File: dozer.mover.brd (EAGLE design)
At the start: 84.8 x 55.9 mm, 12 parts, among them IC1 PIC18F4550_40, U1 L298, U2 L298

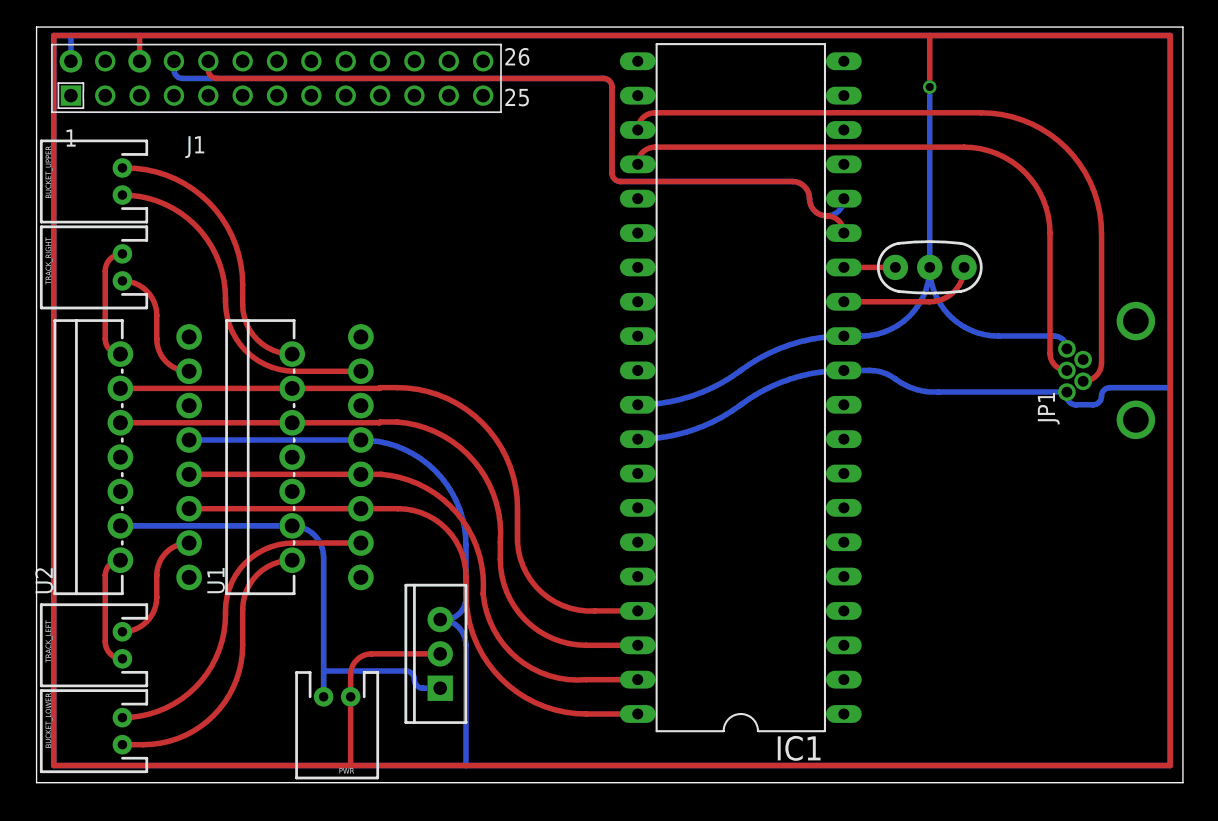
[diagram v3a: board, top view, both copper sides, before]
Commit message: Migrate motor controls further down interface B, frees up GPIO to use for ICSP without having to add loads of resistors. Also added reset circuit required to make PIC run, but not actually a reset switch.
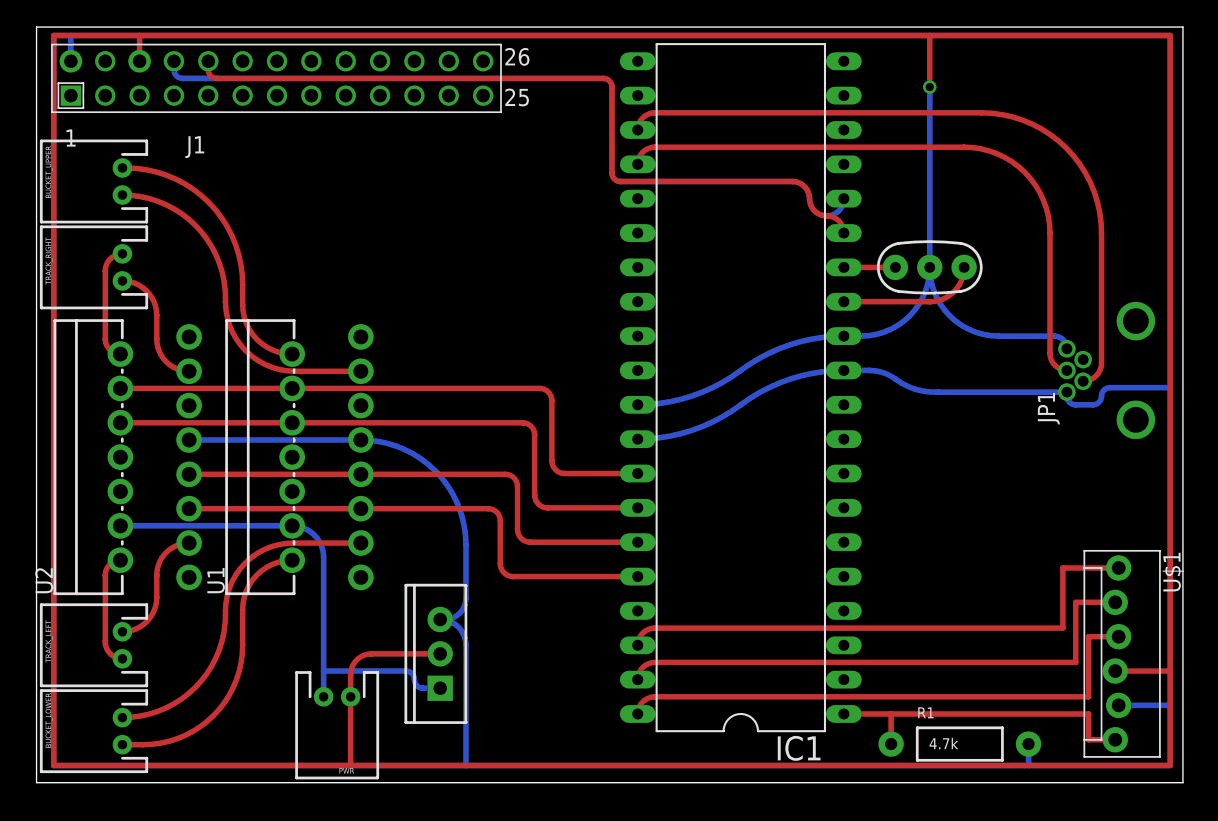
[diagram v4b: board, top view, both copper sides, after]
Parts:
- added R1: 4.7k, SparkFun-Resistors:AXIAL-0.4
- added U$1: PIC-ICSPPOLAR_LOCK, SparkFun-Connectors:MOLEX-1X6_LOCK
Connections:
- removed net N$10: IC1.33
- removed net N$7: IC1.36
- removed net N$8: IC1.35
- removed net N$9: IC1.34
- new net CSSPP: IC1.37
- new net PGC: IC1.39, U$1.2
- new net PGD: IC1.40, U$1.3
- new net PGM: IC1.38, U$1.1
- new net VPP: IC1.1, R1.P$1, U$1.6
- net 5VDC: now also R1.P$2, U$1.5
- net CHAN1+: now also IC1.36; no longer IC1.40
- net CHAN1-: now also IC1.35; no longer IC1.39
- net CHAN2+: now also IC1.34; no longer IC1.38
- net CHAN2-: now also IC1.33; no longer IC1.37
- net GND: now also U$1.4
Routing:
- net PGM: track 0.00 -> 40.5 mm
- net PGD: track 0.00 -> 40.5 mm
- net PGC: track 0.00 -> 40.3 mm
- net VPP: track 0.00 -> 24.2 mm
- net 5VDC: track 358.2 -> 363.6 mm
- net GND: track 343.2 -> 347.3 mm
- net CHAN1+: track 40.2 -> 37.1 mm
- net CHAN2-: track 46.4 -> 43.5 mm
- net CHAN2+: track 46.3 -> 43.5 mm
- net CHAN1-: track 39.5 -> 37.1 mm
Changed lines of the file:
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@@
 <element name="PWR" library="SparkFun-Connectors" package="JST-2-PTH" value="" x="22.225" y="6.35" rot="R180"/>
 <element name="IC2" library="SparkFun-PowerIC" package="TO220-IGO" value="" x="29.845" y="9.525" rot="R90"/>
+<element name="U$1" library="SparkFun-Connectors" package="MOLEX-1X6_LOCK" value="PIC-ICSPPOLAR_LOCK" x="80.01" y="15.875" rot="R270"/>
+<element name="R1" library="SparkFun-Resistors" package="AXIAL-0.4" value="4.7k" x="68.2625" y="2.8575"/>
 </elements>
 <signals>
@@
 <wire x1="7.62" y1="55.245" x2="66.04" y2="55.245" width="0.4064" layer="1"/>
 <wire x1="66.04" y1="55.245" x2="83.82" y2="55.245" width="0.4064" layer="1"/>
-<wire x1="83.82" y1="55.245" x2="83.82" y2="1.27" width="0.4064" layer="1"/>
+<wire x1="83.82" y1="55.245" x2="83.82" y2="8.255" width="0.4064" layer="1"/>
+<wire x1="83.82" y1="8.255" x2="83.82" y2="1.27" width="0.4064" layer="1"/>
 <wire x1="83.82" y1="1.27" x2="23.225" y2="1.27" width="0.4064" layer="1"/>
 <wire x1="23.225" y1="1.27" x2="1.27" y2="1.27" width="0.4064" layer="1"/>
@@
 <wire x1="23.225" y1="7.985" x2="24.765" y2="9.525" width="0.4064" layer="1" curve="-90"/>
 <wire x1="24.765" y1="9.525" x2="29.845" y2="9.525" width="0.4064" layer="1"/>
+<contactref element="U$1" pad="4"/>
+<wire x1="79.756" y1="8.255" x2="83.82" y2="8.255" width="0.4064" layer="1"/>
 </signal>
 <signal name="5VDC">
@@
 <wire x1="2.54" y1="55.245" x2="83.82" y2="55.245" width="0.4064" layer="16"/>
 <wire x1="83.82" y1="55.245" x2="83.82" y2="29.21" width="0.4064" layer="16"/>
-<wire x1="83.82" y1="29.21" x2="83.82" y2="1.27" width="0.4064" layer="16"/>
-<wire x1="83.82" y1="1.27" x2="31.75" y2="1.27" width="0.4064" layer="16"/>
+<wire x1="83.82" y1="29.21" x2="83.82" y2="5.715" width="0.4064" layer="16"/>
+<wire x1="83.82" y1="5.715" x2="83.82" y2="1.27" width="0.4064" layer="16"/>
+<wire x1="83.82" y1="1.27" x2="73.3425" y2="1.27" width="0.4064" layer="16"/>
+<wire x1="73.025" y1="1.27" x2="31.75" y2="1.27" width="0.4064" layer="16"/>
 <wire x1="31.75" y1="1.27" x2="1.27" y2="1.27" width="0.4064" layer="16"/>
 <wire x1="1.27" y1="1.27" x2="1.27" y2="55.245" width="0.4064" layer="16"/>
@@
 <wire x1="29.845" y1="12.065" x2="30.1625" y2="12.065" width="0.4064" layer="16"/>
 <wire x1="30.1625" y1="12.065" x2="31.75" y2="13.6525" width="0.4064" layer="16" curve="90"/>
+<contactref element="U$1" pad="5"/>
+<contactref element="R1" pad="P$2"/>
+<wire x1="80.01" y1="5.715" x2="83.82" y2="5.715" width="0.4064" layer="16"/>
+<wire x1="73.3425" y1="2.8575" x2="73.3425" y2="1.27" width="0.4064" layer="16"/>
+<wire x1="73.3425" y1="1.27" x2="73.025" y2="1.27" width="0.4064" layer="16"/>
 </signal>
 <signal name="USB+">
@@
 <contactref element="U1" pad="5"/>
 <contactref element="U2" pad="5"/>
-<contactref element="IC1" pad="40"/>
 <wire x1="23.98" y1="20.26" x2="11.28" y2="20.26" width="0.4064" layer="1"/>
-<wire x1="23.98" y1="20.26" x2="26.73" y2="20.26" width="0.4064" layer="1"/>
-<wire x1="26.73" y1="20.26" x2="31.75" y2="15.24" width="0.4064" layer="1" curve="-90"/>
-<wire x1="31.75" y1="15.24" x2="31.75" y2="13.97" width="0.4064" layer="1"/>
-<wire x1="31.75" y1="13.97" x2="40.64" y2="5.08" width="0.4064" layer="1" curve="90"/>
-<wire x1="40.64" y1="5.08" x2="44.45" y2="5.08" width="0.4064" layer="1"/>
+<contactref element="IC1" pad="36"/>
+<wire x1="23.98" y1="20.26" x2="33.3975" y2="20.26" width="0.4064" layer="1"/>
+<wire x1="35.2425" y1="15.24" x2="44.45" y2="15.24" width="0.4064" layer="1"/>
+<wire x1="33.3975" y1="20.26" x2="34.29" y2="19.3675" width="0.4064" layer="1" curve="-90"/>
+<wire x1="34.29" y1="19.3675" x2="34.29" y2="16.1925" width="0.4064" layer="1"/>
+<wire x1="35.2425" y1="15.24" x2="34.29" y2="16.1925" width="0.4064" layer="1" curve="-90"/>
 </signal>
 <signal name="CHAN1-">
 <contactref element="U1" pad="7"/>
 <contactref element="U2" pad="7"/>
-<contactref element="IC1" pad="39"/>
 <wire x1="23.98" y1="22.8" x2="11.28" y2="22.8" width="0.4064" layer="1"/>
-<wire x1="23.98" y1="22.8" x2="25.46" y2="22.8" width="0.4064" layer="1"/>
-<wire x1="25.46" y1="22.8" x2="33.02" y2="13.97" width="0.4064" layer="1" curve="-90"/>
-<wire x1="33.02" y1="13.97" x2="40.64" y2="7.62" width="0.4064" layer="1" curve="90"/>
-<wire x1="40.64" y1="7.62" x2="44.45" y2="7.62" width="0.4064" layer="1"/>
+<contactref element="IC1" pad="35"/>
+<wire x1="23.98" y1="22.8" x2="34.6675" y2="22.8" width="0.4064" layer="1"/>
+<wire x1="36.5125" y1="17.78" x2="44.45" y2="17.78" width="0.4064" layer="1"/>
+<wire x1="34.6675" y1="22.8" x2="35.56" y2="21.9075" width="0.4064" layer="1" curve="-90"/>
+<wire x1="35.56" y1="21.9075" x2="35.56" y2="18.7325" width="0.4064" layer="1"/>
+<wire x1="36.5125" y1="17.78" x2="35.56" y2="18.7325" width="0.4064" layer="1" curve="-90"/>
 </signal>
 <signal name="CHAN2+">
 <contactref element="U1" pad="10"/>
 <contactref element="U2" pad="10"/>
-<contactref element="IC1" pad="38"/>
 <wire x1="18.9" y1="26.61" x2="6.2" y2="26.61" width="0.4064" layer="1"/>
-<wire x1="18.9" y1="26.61" x2="25.34" y2="26.61" width="0.4064" layer="1"/>
-<wire x1="25.34" y1="26.61" x2="25.4" y2="26.67" width="0.4064" layer="1" curve="90"/>
-<wire x1="25.4" y1="26.67" x2="26.67" y2="26.67" width="0.4064" layer="1"/>
-<wire x1="26.67" y1="26.67" x2="34.29" y2="17.78" width="0.4064" layer="1" curve="-90"/>
-<wire x1="34.29" y1="17.78" x2="34.29" y2="16.51" width="0.4064" layer="1"/>
-<wire x1="34.29" y1="16.51" x2="40.64" y2="10.16" width="0.4064" layer="1" curve="90"/>
-<wire x1="40.64" y1="10.16" x2="44.45" y2="10.16" width="0.4064" layer="1"/>
+<contactref element="IC1" pad="34"/>
+<wire x1="18.9" y1="26.61" x2="35.9375" y2="26.61" width="0.4064" layer="1"/>
+<wire x1="37.7825" y1="20.32" x2="44.45" y2="20.32" width="0.4064" layer="1"/>
+<wire x1="35.9375" y1="26.61" x2="36.83" y2="25.7175" width="0.4064" layer="1" curve="-90"/>
+<wire x1="36.83" y1="25.7175" x2="36.83" y2="21.2725" width="0.4064" layer="1"/>
+<wire x1="37.7825" y1="20.32" x2="36.83" y2="21.2725" width="0.4064" layer="1" curve="-90"/>
 </signal>
 <signal name="CHAN2-">
 <contactref element="U1" pad="12"/>
 <contactref element="U2" pad="12"/>
-<contactref element="IC1" pad="37"/>
 <wire x1="18.9" y1="29.15" x2="6.2" y2="29.15" width="0.4064" layer="1"/>
-<wire x1="18.9" y1="29.15" x2="25.34" y2="29.15" width="0.4064" layer="1"/>
-<wire x1="25.34" y1="29.15" x2="25.4" y2="29.21" width="0.4064" layer="1" curve="90"/>
-<wire x1="25.4" y1="29.21" x2="26.67" y2="29.21" width="0.4064" layer="1"/>
-<wire x1="26.67" y1="29.21" x2="35.56" y2="20.32" width="0.4064" layer="1" curve="-90"/>
-<wire x1="35.56" y1="20.32" x2="35.56" y2="17.78" width="0.4064" layer="1"/>
-<wire x1="35.56" y1="17.78" x2="41.275" y2="12.7" width="0.4064" layer="1" curve="90"/>
-<wire x1="41.275" y1="12.7" x2="44.45" y2="12.7" width="0.4064" layer="1"/>
+<contactref element="IC1" pad="33"/>
+<wire x1="18.9" y1="29.15" x2="37.2075" y2="29.15" width="0.4064" layer="1"/>
+<wire x1="39.0525" y1="22.86" x2="44.45" y2="22.86" width="0.4064" layer="1"/>
+<wire x1="37.2075" y1="29.15" x2="38.1" y2="28.2575" width="0.4064" layer="1" curve="-90"/>
+<wire x1="38.1" y1="28.2575" x2="38.1" y2="23.8125" width="0.4064" layer="1"/>
+<wire x1="38.1" y1="23.8125" x2="39.0525" y2="22.86" width="0.4064" layer="1" curve="90"/>
 </signal>
 <signal name="BKTL+">
@@
 <signal name="N$28">
 <contactref element="U2" pad="6"/>
-</signal>
-<signal name="N$7">
-<contactref element="IC1" pad="36"/>
-</signal>
-<signal name="N$8">
-<contactref element="IC1" pad="35"/>
-</signal>
-<signal name="N$9">
-<contactref element="IC1" pad="34"/>
-</signal>
-<signal name="N$10">
-<contactref element="IC1" pad="33"/>
 </signal>
 <signal name="UARTTX">
@@
 <wire x1="27.305" y1="8.255" x2="21.225" y2="8.255" width="0.4064" layer="16"/>
 </signal>
+<signal name="CSSPP">
+<contactref element="IC1" pad="37"/>
+</signal>
+<signal name="PGM">
+<contactref element="IC1" pad="38"/>
+<contactref element="U$1" pad="1"/>
+<wire x1="44.45" y1="10.16" x2="45.72" y2="11.43" width="0.4064" layer="1" curve="-90"/>
+<wire x1="45.72" y1="11.43" x2="75.8825" y2="11.43" width="0.4064" layer="1"/>
+<wire x1="75.8825" y1="11.43" x2="75.8825" y2="15.875" width="0.4064" layer="1"/>
+<wire x1="75.8825" y1="15.875" x2="80.01" y2="15.875" width="0.4064" layer="1"/>
+</signal>
+<signal name="PGC">
+<contactref element="IC1" pad="39"/>
+<contactref element="U$1" pad="2"/>
+<wire x1="44.45" y1="7.62" x2="45.72" y2="8.89" width="0.4064" layer="1" curve="-90"/>
+<wire x1="45.72" y1="8.89" x2="76.835" y2="8.89" width="0.4064" layer="1"/>
+<wire x1="76.835" y1="8.89" x2="76.835" y2="13.335" width="0.4064" layer="1"/>
+<wire x1="76.835" y1="13.335" x2="79.756" y2="13.335" width="0.4064" layer="1"/>
+</signal>
+<signal name="PGD">
+<contactref element="IC1" pad="40"/>
+<contactref element="U$1" pad="3"/>
+<wire x1="44.45" y1="5.08" x2="45.72" y2="6.35" width="0.4064" layer="1" curve="-90"/>
+<wire x1="45.72" y1="6.35" x2="77.7875" y2="6.35" width="0.4064" layer="1"/>
+<wire x1="77.7875" y1="6.35" x2="77.7875" y2="10.795" width="0.4064" layer="1"/>
+<wire x1="77.7875" y1="10.795" x2="80.01" y2="10.795" width="0.4064" layer="1"/>
+</signal>
+<signal name="VPP">
+<contactref element="U$1" pad="6"/>
+<contactref element="IC1" pad="1"/>
+<contactref element="R1" pad="P$1"/>
+<wire x1="59.69" y1="5.08" x2="63.1825" y2="5.08" width="0.4064" layer="1"/>
+<wire x1="63.1825" y1="5.08" x2="77.7875" y2="5.08" width="0.4064" layer="1"/>
+<wire x1="77.7875" y1="5.08" x2="77.7875" y2="3.175" width="0.4064" layer="1"/>
+<wire x1="77.7875" y1="3.175" x2="79.756" y2="3.175" width="0.4064" layer="1"/>
+<wire x1="63.1825" y1="2.8575" x2="63.1825" y2="5.08" width="0.4064" layer="1"/>
+</signal>
 </signals>
